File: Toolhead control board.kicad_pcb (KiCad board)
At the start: 2 copper layers, 51.6 x 31.4 mm, 53 parts, among them J1 Conn_01x02_Pin, J12 Conn_01x04_Male, J2 Conn_01x02_Pin, J3 Conn_01x06_Pin, J4 Conn_01x02_Pin, J5 Conn_01x02_Pin, J6 Conn_01x02_Pin, J7 USB_C_Receptacle_USB2.0_14P, Q1 AS3400, Q2 AS3400, Q3 AS3400, U1 ADXL345, U2 STM32F042G6Ux, U3 TMC2209, U4 AP63205WU, U5 MCP1802x-xx02xOT, Y1 8MHz

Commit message: Rev1. Uart interface
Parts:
- removed J7: USB_C_Receptacle_USB2.0_14P, Connector_USB:USB_C_Receptacle_GCT_USB4085
- removed R10, R11, R5: OPEN, Resistor_SMD:R_0805_2012Metric
- removed R17, R20: 5.1k, Resistor_SMD:R_0805_2012Metric
- added C13: C, Capacitor_SMD:C_0805_2012Metric, B.Cu at (152.7, 86.8)
- added C14: 10uF, Capacitor_SMD:C_0805_2012Metric, F.Cu at (162.0, 82.2)
- added C15: 1uF, Capacitor_SMD:C_0805_2012Metric, B.Cu at (146.8, 86.4)
- added C16: 1uF, Capacitor_SMD:C_0805_2012Metric, F.Cu at (138.2, 84.7)
- added C17: 4.7uF, Capacitor_SMD:C_0805_2012Metric, F.Cu at (142.5, 89.2)
- added J13: Conn_01x04_Male, Connector_JST:JST_XH_S4B-XH-A-1_1x04_P2.50mm_Horizontal, F.Cu at (153.8, 91.8)
- added J14: Conn_01x04_Male, Connector_JST:JST_XH_S3B-XH-A-1_1x03_P2.50mm_Horizontal, F.Cu at (138.8, 76.8)
- added R21: OPEN, Resistor_SMD:R_0805_2012Metric, B.Cu at (135.5, 87.0)
- added R22: OPEN, Resistor_SMD:R_0805_2012Metric, B.Cu at (133.2, 87.0)
- added R23: OPEN, Resistor_SMD:R_0805_2012Metric, B.Cu at (134.8, 81.2)
- added R24: OPEN, Resistor_SMD:R_0805_2012Metric, B.Cu at (136.8, 79.0)
- added R25: OPEN, Resistor_SMD:R_0805_2012Metric, B.Cu at (137.5, 74.5)
- added R6: 22k, Resistor_SMD:R_0805_2012Metric, B.Cu at (141.0, 77.7)
- added REF**: TestPoint_Pad_1.5x1.5mm, TestPoint:TestPoint_Pad_1.5x1.5mm, F.Cu at (140.0, 89.8)
- added REF**: TestPoint_Pad_1.5x1.5mm, TestPoint:TestPoint_Pad_1.5x1.5mm, B.Cu at (135.0, 84.2)
- added REF**: TestPoint_Pad_1.5x1.5mm, TestPoint:TestPoint_Pad_1.5x1.5mm, F.Cu at (142.0, 85.8)
- added REF**: TestPoint_Pad_1.5x1.5mm, TestPoint:TestPoint_Pad_1.5x1.5mm, F.Cu at (135.2, 91.8)
- added REF**: TestPoint_Pad_1.5x1.5mm, TestPoint:TestPoint_Pad_1.5x1.5mm, B.Cu at (163.2, 86.5)
- added REF**: TestPoint_Pad_1.5x1.5mm, TestPoint:TestPoint_Pad_1.5x1.5mm, B.Cu at (170.8, 97.2)
- added SW1: SW_SPST, Button_Switch_SMD:SW_SPST_B3U-1000P, B.Cu at (150.0, 74.0)
- added SW2: SW_SPST, Button_Switch_SMD:SW_SPST_B3U-1000P, F.Cu at (138.0, 82.0)
- added TP1: TestPoint_Probe, TestPoint:TestPoint_Pad_D1.0mm, B.Cu at (152.6, 82.6)
- added TP2: TestPoint_Probe, TestPoint:TestPoint_Pad_D1.0mm, B.Cu at (154.3, 77.3)
- added TP3: TestPoint_Probe, TestPoint:TestPoint_Pad_D1.0mm, B.Cu at (148.7, 79.2)
- C10, C11, C2, C4, C5, C6, C9, L1, Q1, Q2, Q3, R1, R13, R14, R15, R16, R2, R4, R7, R8, R9, U1, U2, U3, U4, Y1: moved to B.Cu
- C7, J1, J2, J4, J5, J6: moved to F.Cu
- J12: footprint Connector_JST:JST_XH_B4B-XH-A_1x04_P2.50mm_Vertical -> Connector_JST:JST_XH_S4B-XH-A-1_1x04_P2.50mm_Horizontal
- J3: value Conn_01x06_Pin -> Conn_01x02_Pin; footprint Connector_PinHeader_2.54mm:PinHeader_1x06_P2.54mm_Vertical -> Connector_JST:JST_XH_S2B-XH-A-1_1x02_P2.50mm_Horizontal
- R3: value 27 -> 4.7k; moved to B.Cu
- moved R16 40.2 mm to (170.5, 93.2)
- moved J2 37.5 mm to (131.8, 89.8)
- moved Q3 37.4 mm to (170.0, 86.5), turned to -90 degrees
- moved J1 37.1 mm to (131.8, 82.0)
- moved Q1 37.1 mm to (128.2, 90.0), turned to 90 degrees
- moved R14 36.5 mm to (166.0, 83.5), turned to 90 degrees
- moved R13 35.9 mm to (134.5, 94.5), turned to -90 degrees
- moved R4 34.4 mm to (128.2, 93.5), turned to 180 degrees
- moved R15 33.5 mm to (166.2, 87.0), turned to -45 degrees
- moved C3 32.8 mm to (138.8, 94.2)
- moved J6 32.6 mm to (168.2, 91.8)
- moved R12 29.8 mm to (142.5, 93.0), turned to -90 degrees
- moved J3 27.9 mm to (168.2, 83.5), turned to 90 degrees
- moved R18 25.0 mm to (163.8, 74.0), turned to 180 degrees
- moved R19 24.3 mm to (158.8, 74.0), turned to 180 degrees
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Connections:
- C1 pad 1: THERMISTOR -> THERMISTOR_1
- J1 pad 1: GND -> THERMISTOR_1
- J1 pad 2: THERMISTOR -> GND
- J3 pad 1: Net-(J3-Pin_1) -> THERMISTOR_2
- J3 pad 2: Net-(J3-Pin_2) -> GND
- J5 pad 2: Net-(J5-Pin_2) -> Net-(J4-Pin_2)
- Q2 pad 3: Net-(J4-Pin_1) -> Net-(J4-Pin_2)
- R1 pad 2: THERMISTOR -> THERMISTOR_1
- R12 pad 2: Net-(J5-Pin_2) -> Net-(J4-Pin_1)
- R13 pad 2: Net-(J5-Pin_2) -> Net-(J4-Pin_1)
- R2 pad 2: D- -> TX
- R3 pad 1: Net-(U2-PA10/PA12) -> +3.3V
- R3 pad 2: D+ -> THERMISTOR_2
- U1 pad 8: unconnected-(U1-INT1-Pad8) -> ADXL_INT
- U2 pad 1: unconnected-(U2-PB8-Pad1) -> Net-(SW2-B)
- U2 pad 14: THERMISTOR -> THERMISTOR_2
- U2 pad 15: HEATER -> HOTEND_FAN
- U2 pad 20: Net-(U2-PA10/PA12) -> RX
- U2 pad 21: Net-(J3-Pin_4) -> PART_FAN
- U2 pad 22: Net-(J3-Pin_2) -> HEATER
- U2 pad 27: unconnected-(U2-PB6-Pad27) -> ADXL_INT
- U2 pad 28: unconnected-(U2-PB7-Pad28) -> PROBE
- U2 pad 4: NRST -> Net-(SW1-B)
- U2 pad 6: HOTEND_FAN -> THERMISTOR_1
- U2 pad 7: PART_FAN -> Net-(U2-PA1)
- U3 pad 1: Net-(J12-Pin_4) -> Net-(J12-Pin_1)
- U3 pad 15: +3V3 -> +3.3V
- U3 pad 21: Net-(J12-Pin_1) -> Net-(J12-Pin_4)
- U3 pad 24: Net-(J12-Pin_2) -> Net-(J12-Pin_3)
- U3 pad 26: Net-(J12-Pin_3) -> Net-(J12-Pin_2)
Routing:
- net +5V: track 104.6 -> 19.9 mm, vias 1 -> 4
- net +VDC: track 92.4 -> 17.0 mm, vias 3 -> 8
- net Net-(J4-Pin_2): track 4.43 -> 45.8 mm
- net THERMISTOR: track 37.9 -> 0.00 mm, vias 2 -> 0
- net THERMISTOR_1: track 0.00 -> 33.6 mm
- net THERMISTOR_2: track 0.00 -> 24.0 mm
- net GND: track 17.4 -> 36.7 mm, vias 0 -> 81
- net HOTEND_FAN: track 8.23 -> 26.5 mm
- net Net-(J12-Pin_1): track 26.8 -> 10.6 mm
- net Net-(J12-Pin_2): track 19.3 -> 6.23 mm
- net PROBE: track 0.00 -> 12.0 mm
- net Net-(J14-Pin_3): track 0.00 -> 11.8 mm
- net Net-(J12-Pin_3): track 16.3 -> 5.31 mm
- net NRST: track 10.6 -> 0.00 mm
- net Net-(J3-Pin_4): track 10.6 -> 0.00 mm
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- added copper zone on B.Cu, net +3.3V
- added copper zone on B.Cu, net +5V
- added copper zone on F.Cu, net +5V
- added copper zone on B.Cu, net +VDC
- added copper zone on F.Cu, net +VDC
- added copper zone on B.Cu, net GND
- added copper zone on F.Cu, net GND
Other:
- board size 51.6 x 31.4 mm -> 52 x 39.5 mm
- board text added: "+"
- board text added: "-"
- board text added: "3.3V"
- board text added: "5V"
- board text added: "BOOT"
- board text added: "GND"
- board text added: "HEATER"
- board text added: "HOST"
- board text added: "HOT- FAN END"
- board text added: "HOT. FAN"
- board text added: "HOTEND FAN"
- board text added: "MOTOR"
- board text added: "P. FAN"
- board text added: "PART FAN"
- board text added: "PROBE"
- board text added: "RESET"
- board text added: "RX"
- board text added: "THERM 1"
- board text added: "THERM 2"
- board text added: "THERMISTOR 1"
- board text added: "THERMISTOR 2"
- board text added: "TX"
- board text added: "V+"
- board text added: "VORON 0 TOOLHEAD BOARD REV 1 ©2025 3D OLYMPICS"
- board text added: "X"
- board text added: "Y"
- board text added: "Z"

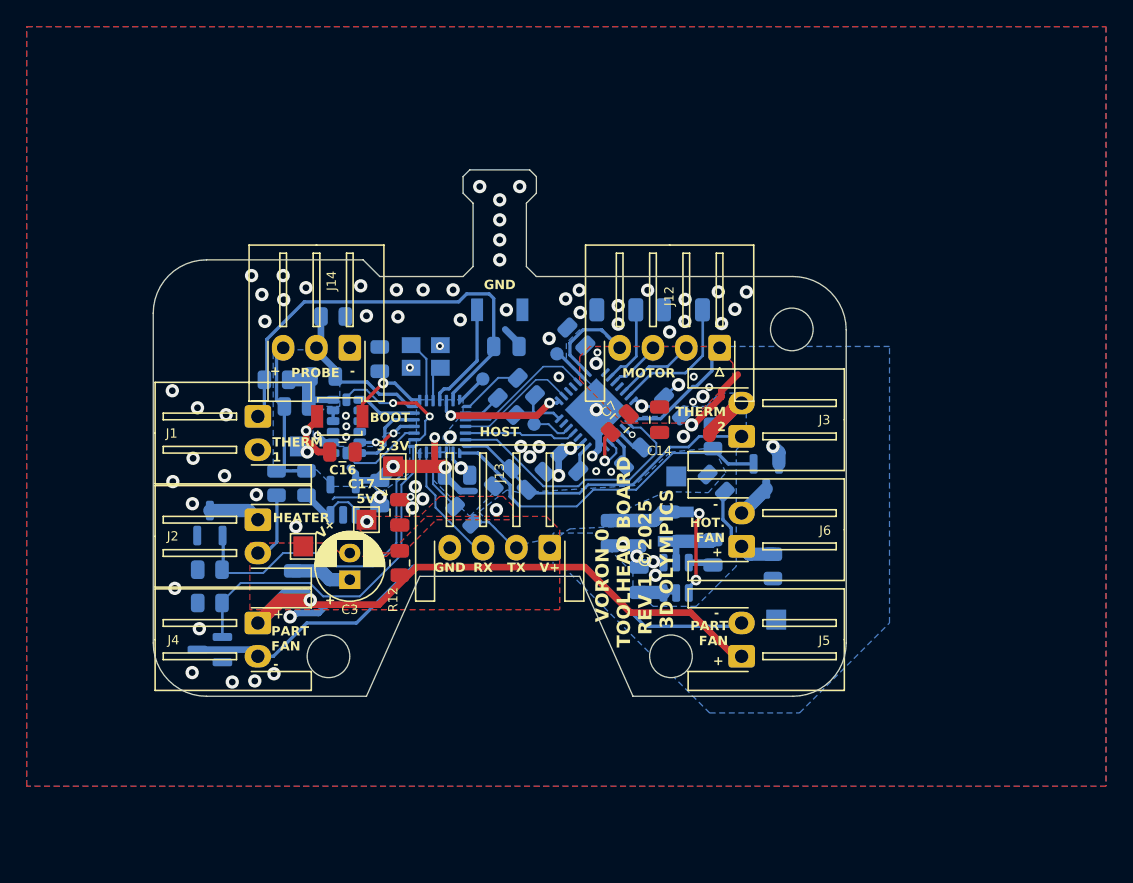
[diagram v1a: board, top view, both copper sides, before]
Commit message: Rev2 (USB) largely done
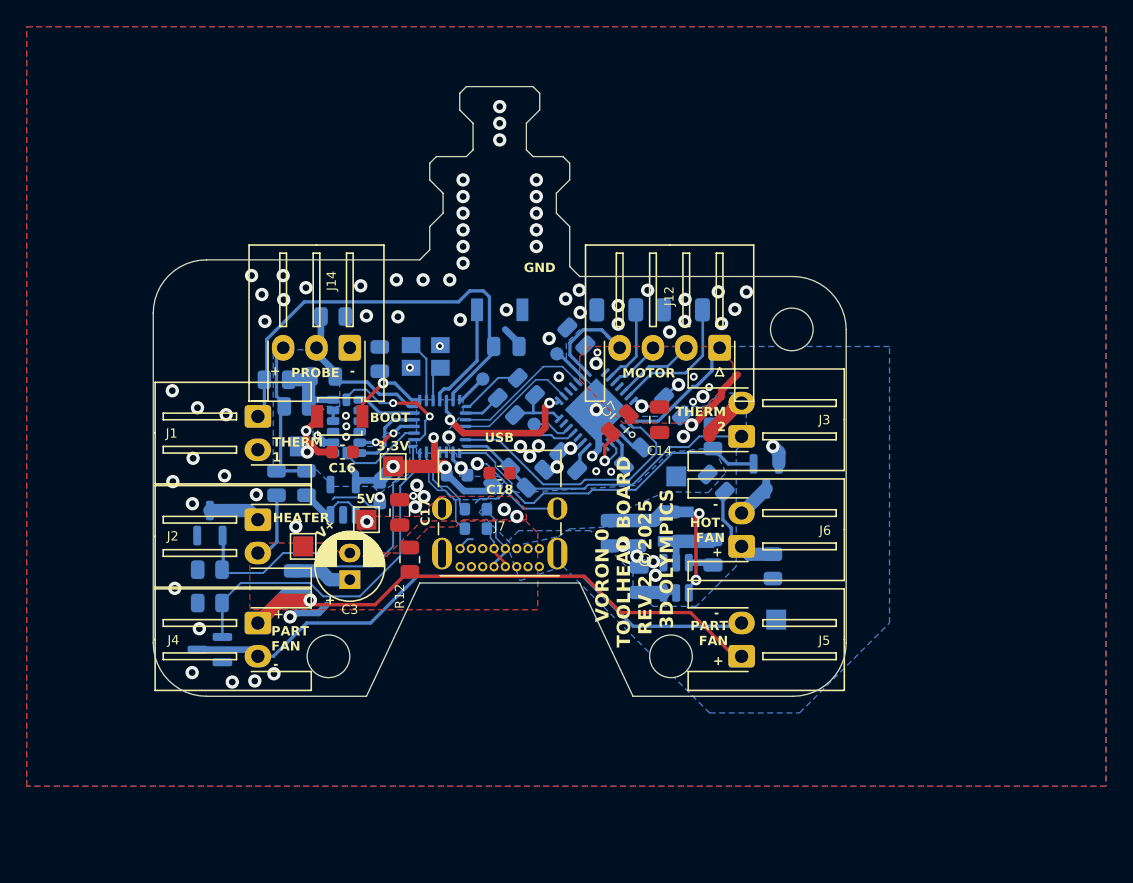
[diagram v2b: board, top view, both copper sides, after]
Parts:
- removed J13: Conn_01x04_Male, Connector_JST:JST_XH_S4B-XH-A-1_1x04_P2.50mm_Horizontal
- added C18: 1uF, Capacitor_SMD:C_0603_1608Metric, F.Cu at (150.0, 86.2)
- added J7: USB_C_Receptacle_USB2.0_14P, Connector_USB:USB_C_Receptacle_GCT_USB4085, F.Cu at (153.0, 93.3)
- added R5: 27, Resistor_SMD:R_0603_1608Metric, B.Cu at (148.2, 90.4)
- added REF**: MountingHole_2.2mm_M2, MountingHole:MountingHole_2.2mm_M2, F.Cu at (150.0, 67.0)
- C12, C15, C16: footprint Capacitor_SMD:C_0805_2012Metric -> Capacitor_SMD:C_0603_1608Metric
- R2: footprint Resistor_SMD:R_0805_2012Metric -> Resistor_SMD:R_0603_1608Metric
- moved R2 1.02 mm to (148.2, 89.0), turned to 0 degrees
- moved R12 0.79 mm to (143.2, 92.8)
- moved C13 0.16 mm to (152.7, 86.7)
- moved R3 0.12 mm to (150.2, 86.5)
- moved C8 0.11 mm to (155.1, 85.3)
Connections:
- R2 pad 2: TX -> D-
- U2 pad 20: RX -> Net-(U2-PA10/PA12)
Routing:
- net GND: track 36.7 -> 47.7 mm, vias 81 -> 90
- net RX: track 9.25 -> 0.00 mm
- net Net-(U2-PA10/PA12): track 0.00 -> 7.32 mm
- net D-: track 0.00 -> 5.24 mm
- net TX: track 4.15 -> 0.00 mm
- net +3.3V: track 34.8 -> 38.6 mm
- net D+: track 0.00 -> 3.43 mm
- net Net-(U2-PA9/PA11): track 4.76 -> 5.60 mm
- net Net-(J4-Pin_2): track 45.8 -> 45.2 mm
- net +5V: vias 4 -> 5
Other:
- board size 52 x 39.5 mm -> 52 x 45.8 mm
- board text added: "USB"
- board text added: "VORON 0 TOOLHEAD BOARD REV 2 ©2025 3D OLYMPICS"
- board text removed: "HOST"
- board text removed: "RX"
- board text removed: "TX"
- board text removed: "VORON 0 TOOLHEAD BOARD REV 1 ©2025 3D OLYMPICS"

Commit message: Rev2, as ordered
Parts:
- added C19: 4.7uF, Capacitor_SMD:C_0805_2012Metric, B.Cu at (134.6, 84.8)
- added C20: 1uF, Capacitor_SMD:C_0603_1608Metric, B.Cu at (135.8, 78.8)
- added U6: LP5907-2.5, Package_TO_SOT_SMD:SOT-23-5, B.Cu at (134.8, 81.6)
- R23, R24: moved to F.Cu
- moved R1 16.6 mm to (149.7, 77.0), turned to 0 degrees
- moved R21 7.59 mm to (128.2, 84.8), turned to 180 degrees
- moved C1 6.98 mm to (146.0, 71.5), turned to 90 degrees
- moved R22 5.15 mm to (128.2, 88.2), turned to 180 degrees
- moved REF** 3.04 mm to (135.4, 87.3)
- moved SW2 2.38 mm to (138.1, 84.4)
- moved C16 2.37 mm to (137.8, 87.0)
- moved R24 2.06 mm to (137.2, 81.0), turned to 90 degrees
- moved Q1 1.75 mm to (128.2, 91.8), turned to 0 degrees
- moved R23 1.43 mm to (134.7, 82.7), turned to 90 degrees
- moved R4 1.25 mm to (128.2, 94.8)
- moved R8 1.00 mm to (128.2, 97.0)
- moved Q2 0.50 mm to (128.2, 100.0)
- moved REF** 0.50 mm to (135.2, 91.2)
- moved Y1 0.50 mm to (144.4, 77.0)
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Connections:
- J2 pad 1: Net-(J2-Pin_1) -> +VDC
- J2 pad 2: +VDC -> Net-(J2-Pin_2)
- J7 pad A5: Net-(J7-CC1) -> unconnected-(J7-CC1-PadA5)
- J7 pad B5: Net-(J7-CC2) -> unconnected-(J7-CC2-PadB5)
- Q1 pad 3: Net-(J2-Pin_1) -> Net-(J2-Pin_2)
- U1 pad 6: +3.3V -> +2V5
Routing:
- net Net-(J14-Pin_3): track 11.6 -> 19.4 mm
- net +3.3V: track 38.6 -> 33.2 mm, vias 7 -> 8
- net +2V5: track 0.00 -> 4.34 mm
- net Net-(J2-Pin_1): track 3.88 -> 0.00 mm
- net PROBE: track 12.0 -> 15.2 mm
- net Net-(J2-Pin_2): track 0.00 -> 2.87 mm
- net Net-(SW2-B): track 7.51 -> 9.87 mm
- net GND: track 47.7 -> 50.0 mm, vias 90 -> 101
- net +5V: track 19.9 -> 17.8 mm
- net +VDC: track 17.0 -> 15.0 mm
- net THERMISTOR_1: track 33.6 -> 35.2 mm
- net PART_FAN: track 27.1 -> 26.0 mm
- net Net-(SW1-B): track 8.19 -> 7.20 mm
- net Net-(U2-PF1): track 2.69 -> 3.19 mm
- net Net-(U2-PF0): track 4.71 -> 5.21 mm
- added copper zone on F.Cu, net +3.3V
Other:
- board text added: "EXTRUDER MOTOR"
- board text added: "P.FAN"
- board text added: "SCREW MUST FIT PAST"
- board text added: "TH.1"
- board text added: "TOP OF MOTOR MOUNTS, STATIONARY AT BACK"
- board text added: "X CARRIAGE"
- board text removed: "HOT- FAN END"
- board text removed: "P. FAN"
